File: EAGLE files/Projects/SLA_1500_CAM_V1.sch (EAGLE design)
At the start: 33 parts, among them J5 MOLEX 53398-04

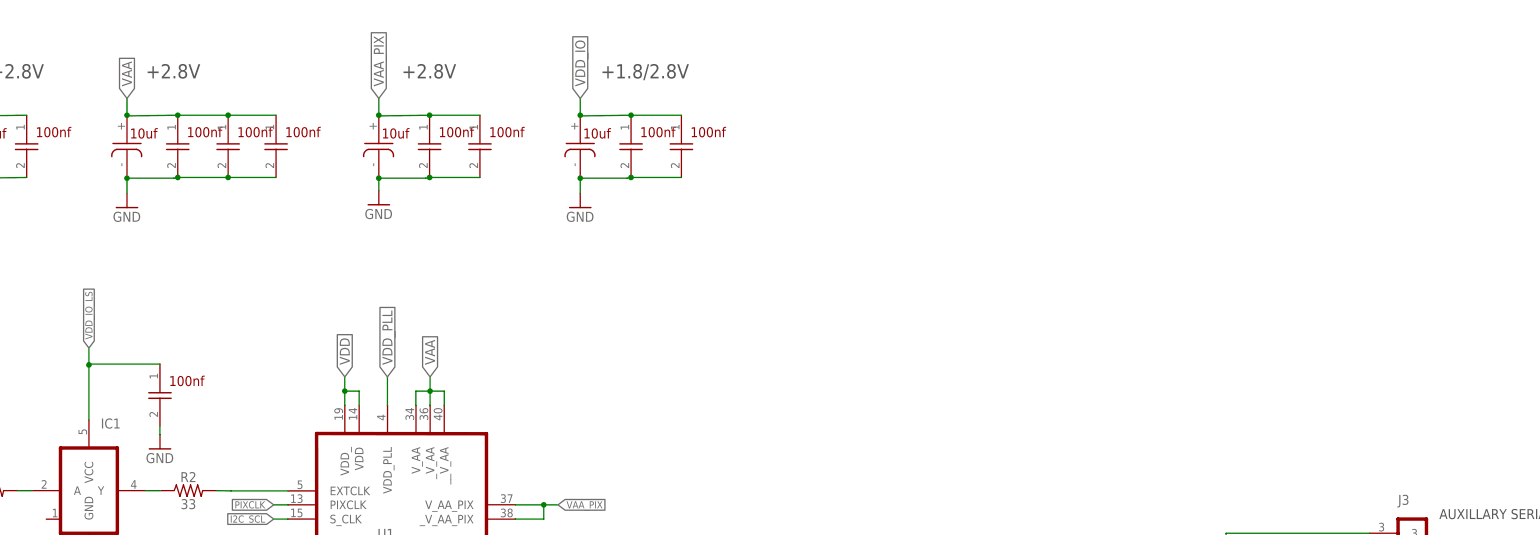
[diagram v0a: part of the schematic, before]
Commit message: Update SLA_1500_CAM schem
Created Devices, symbols, and footprints for power management
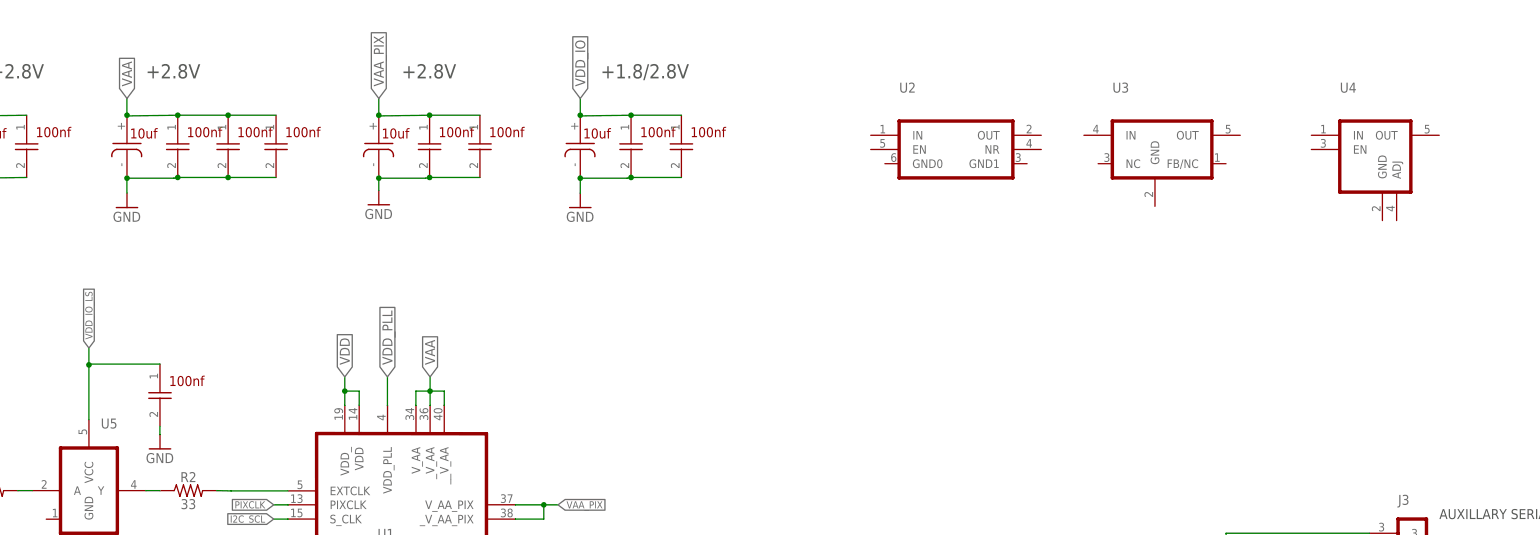
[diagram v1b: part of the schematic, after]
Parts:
- added U2: (no value), Sightline:TPS73633DCQR
- added U3: (no value), Sightline:TPS71518DCKR
- added U4: (no value), Sightline:AP7331-WG-7
- renumbered IC1 to U5
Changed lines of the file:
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@@
 <setting verticaltext="up"/>
 </settings>
-<grid distance="0.1" unitdist="inch" unit="inch" style="lines" multiple="1" display="no" altdistance="0.01" altunitdist="inch" altunit="inch"/>
+<grid distance="0.1" unitdist="inch" unit="inch" style="lines" multiple="1" display="yes" altdistance="0.01" altunitdist="inch" altunit="inch"/>
 <layers>
 <layer number="1" name="Top" color="4" fill="1" visible="no" active="no"/>
@@
 <part name="GND9" library="supply1" library_urn="urn:adsk.eagle:library:371" deviceset="GND" device=""/>
 <part name="GND10" library="supply1" library_urn="urn:adsk.eagle:library:371" deviceset="GND" device=""/>
-<part name="IC1" library="Sightline" deviceset="SN74AUC1G17" device=""/>
 <part name="GND11" library="supply1" library_urn="urn:adsk.eagle:library:371" deviceset="GND" device=""/>
 <part name="R1" library="SparkFun-Resistors" library_urn="urn:adsk.eagle:library:532" deviceset="RESISTOR" device="0402" package3d_urn="urn:adsk.eagle:package:39657/1" value="33"/>
@@
 <part name="J5" library="Sightline" deviceset="MOLEX_53398-04" device="" value="MOLEX 53398-04"/>
 <part name="J6" library="Sightline" deviceset="MOLEX_53398-04" device=""/>
+<part name="U2" library="Sightline" deviceset="TPS73633DCQR" device=""/>
+<part name="U3" library="Sightline" deviceset="TPS71518DCKR" device=""/>
+<part name="U4" library="Sightline" deviceset="AP7331-WG-7" device=""/>
+<part name="U5" library="Sightline" deviceset="SN74AUC1G17" device=""/>
 </parts>
 <sheets>
@@
 <attribute name="VALUE" x="12.7" y="162.40125" size="1.778" layer="96"/>
 </instance>
-<instance part="IC1" gate="G$1" x="76.2" y="185.42" smashed="yes">
-<attribute name="NAME" x="78.308" y="196.522" size="1.778" layer="95"/>
-</instance>
 <instance part="GND11" gate="1" x="76.2" y="165.1" smashed="yes">
 <attribute name="VALUE" x="73.66" y="162.56" size="1.778" layer="96"/>
@@
 <instance part="J6" gate="G$1" x="309.88" y="73.66" smashed="yes" rot="MR180">
 <attribute name="NAME" x="307.34" y="63.5" size="1.778" layer="95" rot="MR180"/>
+</instance>
+<instance part="U2" gate="G$1" x="231.14" y="246.38" smashed="yes">
+<attribute name="NAME" x="220.98" y="256.54" size="1.778" layer="95"/>
+</instance>
+<instance part="U3" gate="G$1" x="266.7" y="246.38" smashed="yes">
+<attribute name="NAME" x="259.08" y="256.54" size="1.778" layer="95"/>
+</instance>
+<instance part="U4" gate="G$1" x="302.26" y="241.3" smashed="yes">
+<attribute name="NAME" x="299.72" y="256.54" size="1.778" layer="95"/>
+</instance>
+<instance part="U5" gate="G$1" x="76.2" y="185.42" smashed="yes">
+<attribute name="NAME" x="78.308" y="196.522" size="1.778" layer="95"/>
 </instance>
 </instances>
@@
 <segment>
 <pinref part="GND11" gate="1" pin="GND"/>
-<pinref part="IC1" gate="G$1" pin="GND"/>
 <wire x1="76.2" y1="167.64" x2="76.2" y2="172.7" width="0.1524" layer="91"/>
+<pinref part="U5" gate="G$1" pin="GND"/>
 </segment>
 <segment>
@@
 <segment>
 <pinref part="R1" gate="G$1" pin="2"/>
-<pinref part="IC1" gate="G$1" pin="A"/>
 <wire x1="63.5" y1="185.42" x2="66.0715625" y2="185.42" width="0.1524" layer="91"/>
+<pinref part="U5" gate="G$1" pin="A"/>
 </segment>
 </net>
 <net name="VDD_IO_LS" class="0">
 <segment>
-<pinref part="IC1" gate="G$1" pin="VCC"/>
 <wire x1="76.2" y1="198.084375" x2="76.2" y2="207.883125" width="0.1524" layer="91"/>
 <label x="76.2" y="210.899375" size="1.27" layer="95" rot="R90" xref="yes"/>
@@
 <wire x1="76.04125" y1="207.883125" x2="76.2" y2="207.883125" width="0.1524" layer="91"/>
 <junction x="76.2" y="207.883125"/>
+<pinref part="U5" gate="G$1" pin="VCC"/>
 </segment>
 </net>
 <net name="N$13" class="0">
 <segment>
-<pinref part="IC1" gate="G$1" pin="Y"/>
 <pinref part="R2" gate="G$1" pin="1"/>
 <wire x1="86.368125" y1="185.42" x2="88.9" y2="185.42" width="0.1524" layer="91"/>
-</segment>
-</net>
+<pinref part="U5" gate="G$1" pin="Y"/>
+</segment>
+</net>

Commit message: Update SLA_1500_CAM schem
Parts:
- removed C1, C2, C3, C5: 10uf, Sightline:CAP3216-18LOW_ESR
- removed C4: 10u, Sightline:CAP3216-18LOW_ESR
- added C18, C19, C20, C28, C29: 10uf, Seeed-Capacitor:TANTALUM-SMD-10UF-10V-10%(AVX-A)
- added C21: 470nF, SparkFun-Capacitors:470NF-0402-16V-10%
- added C22: 10nf, Seeed-Capacitor:CERAMIC-10NF-50V-10%-X7R(0402)
- added C23, C24, C25, C26: 1uf, Seeed-Capacitor:CERAMIC-1UF-10V-10%-X5R(0402)
- added C27: 100nf, Seeed-Capacitor:CERAMIC-100NF-25V-10%-X7R(0402)
- added R8: 60.2K, SparkFun-Resistors:62KOHM-0603-1/10W-5%
- added R9: 10k, SparkFun-Resistors:10KOHM-0603-1/10W-1%
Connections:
- net FRAME_VALID renamed N$1
- net LINE_VALID renamed N$2
- net PIXCLK renamed N$3
- removed net +3.3V: J5.1
- removed net +5V: J1.P_5V_0, J1.P_5V_1, J2.1, J6.1, J6.2
- removed net AUX_3V3: C6.P$1, OSC1.NH, OSC1.VCC
- new net N$21: C22.2, U2.NR
- new net N$23: R8.1, R9.2, U4.ADJ
- new net P1P8V: C21.1, U3.OUT
- new net P2P8V: C26.2, R8.2, U4.OUT
- new net P3P3V: C24.2, C27.2, C6.P$1, J5.1, OSC1.NH, OSC1.VCC, U2.OUT, U3.IN
- new net P5V: C23.2, C25.2, J1.P_5V_0, J1.P_5V_1, J2.1, J6.1, J6.2, U2.EN, U2.IN, U4.EN, U4.IN
- net GND: now also C18.-, C19.-, C20.-, C21.2, C22.1, C23.1, C24.1, C25.1, C26.1, C27.1, C28.-, C29.-, R9.1, U1.A_GND(0), U1.A_GND(1), U1.D_GND(0), U1.D_GND(1), U1.D_GND(2), U2.GND0, U2.GND1, U3.GND, U4.GND; no longer C1.2, C2.2, C3.2, C4.2, C5.2, U1.A_GND, U1.D_GND, U1._A_GND, U1._D_GND, U1.__D_GND
- net VAA: now also C18.+, U1.V_AA(0), U1.V_AA(1), U1.V_AA(2); no longer C3.1, U1.V_AA, U1._V_AA, U1.__V_AA
- net VAA_PIX: now also C20.+, U1.V_AA_PIX(0), U1.V_AA_PIX(1); no longer C4.1, U1.V_AA_PIX, U1._V_AA_PIX
- net VDD: now also C19.+, U1.VDD(0), U1.VDD(1); no longer C1.1, U1.VDD, U1.VDD_
- net VDD_IO: now also C28.+, U1.VDD_IO(0), U1.VDD_IO(1); no longer C5.1, U1.VDD_IO, U1.VDD_IO_
- net VDD_PLL: now also C29.+; no longer C2.1
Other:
- note added: "3.3V to 1.8V SUPPLY"
- note added: "5V to 2.8V SUPPLY"
- note added: "5V to 3.3V SUPPLY"
- note removed: "+1.8V"
- moved on the sheet: J1, J2, J3, J4, J5, J6, OSC1, R1, R2, R3, R4, R5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

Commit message: Update SLA_1500_CAM schem
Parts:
- added C1, C2, C3, C4, C5: 10uf, Seeed-Capacitor:TANTALUM-SMD-10UF-10V-10%(AVX-A)
- added C30, C31: 100nf, Seeed-Capacitor:CERAMIC-100NF-25V-10%-X7R(0402)
- added JP1, JP2, JP3, JP4, JP5: JUMPER_NC, SparkFun-Jumpers:JUMPER-SMT_2_NC_TRACE_SILK
- added LED1: (no value), led:LEDCHIP-LED0603
- added R10: 10k, SparkFun-Resistors:10KOHM-0603-1/10W-1%
- added R11: 680, SparkFun-Resistors:680OHM-0603-1/10W-5%
- added S1: SPST, SparkFun-Switches:MOMENTARY-SWITCH-SPST-SMD-4.6X2.8MM
- added U6: (no value), Sightline:CAT811
- added U7: (no value), Sightline:SN74AUC1G08
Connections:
- new net N$27: S1.2, U6.MR_BAR
- new net N$28: U6.RESET_BAR, U7.B
- new net N$29: U1.RESET_BAR, U7.Y
- new net N$30: LED1.A, R11.1
- new net SLA_RESET_BAR: R10.1, U7.A
- net GND: now also C1.-, C2.-, C3.-, C30.1, C31.1, C4.-, C5.-, LED1.C, S1.1, U6.GND, U7.GND
- net P1P8V: now also JP1.1
- net P2P8V: now also JP2.1, JP3.1, JP4.1, JP5.1
- net P3P3V: now also C30.2, U6.VCC
- net P5V: now also R11.2
- net VAA: now also C3.+, JP3.2
- net VAA_PIX: now also C4.+, JP4.2
- net VDD: now also C1.+, JP1.2
- net VDD_IO: now also C5.+, J1.VIOSEL, JP5.2
- net VDD_IO_LS: now also C31.2, R10.2, U7.VCC
- net VDD_PLL: now also C2.+, JP2.2
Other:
- moved on the sheet: C18, C19, C20, C25, C26, C28, C29, J1, J2, J3, J4, J5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
